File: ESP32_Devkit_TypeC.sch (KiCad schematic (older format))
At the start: 39 parts, among them J1 USB_C_Receptacle_USB2.0, J2 Conn_01x19, J3 Conn_01x19, Q1 SS8050, Q2 SS8050, SW1 EN, SW2 BOOT, U1 MP2451, U2 CH340G, U3 ESP32-PICO-D4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

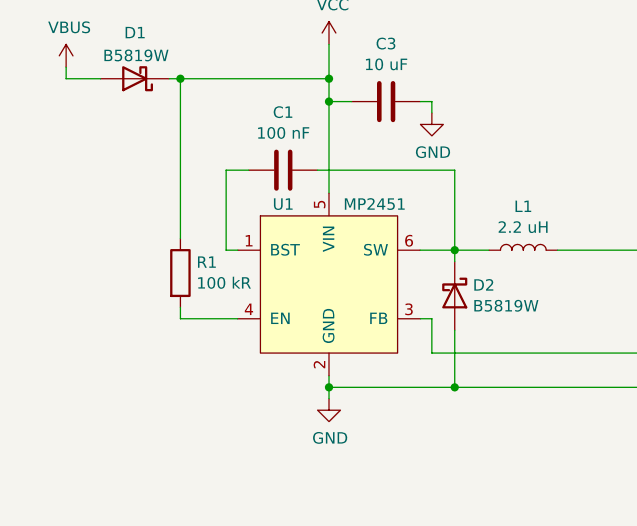
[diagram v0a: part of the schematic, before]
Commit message: Increase strength of step down enable pullup
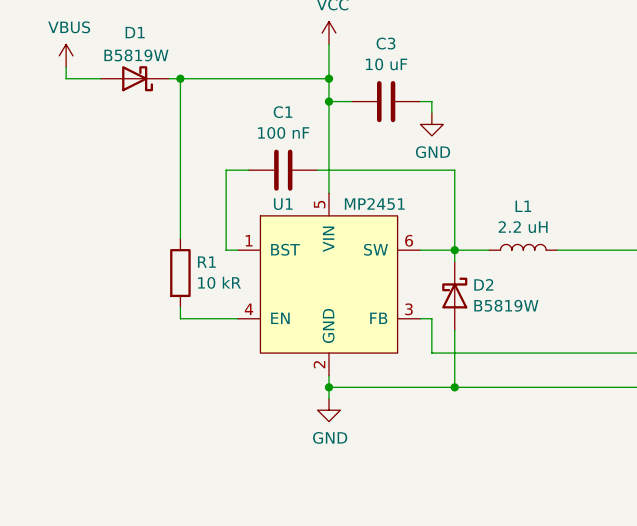
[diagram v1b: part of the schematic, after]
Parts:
- R1: value 100 kR -> 10 kR; LCSC C25741 -> C25744
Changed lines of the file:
@@
 P 1550 5100
 F 0 "R1" H 1620 5146 50  0000 L CNN
-F 1 "100 kR" H 1620 5055 50  0000 L CNN
+F 1 "10 kR" H 1620 5055 50  0000 L CNN
 F 2 "Resistor_SMD:R_0402_1005Metric" V 1480 5100 50  0001 C CNN
 F 3 "~" H 1550 5100 50  0001 C CNN
-F 4 "C25741" H 1550 5100 50  0001 C CNN "LCSC"
+F 4 "C25744" H 1550 5100 50  0001 C CNN "LCSC"
 	1    1550 5100
 	1    0    0    -1

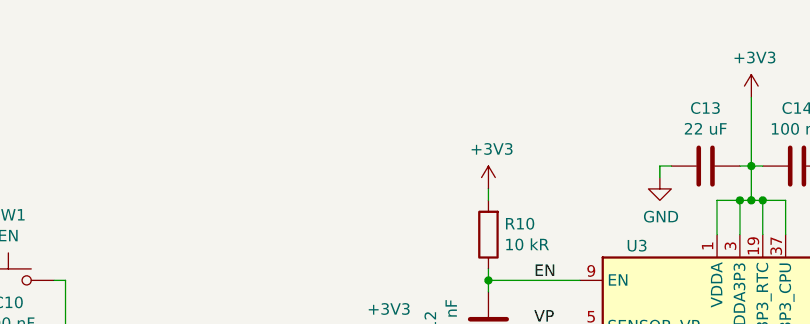
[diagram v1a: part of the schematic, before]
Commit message: Add tooling holes
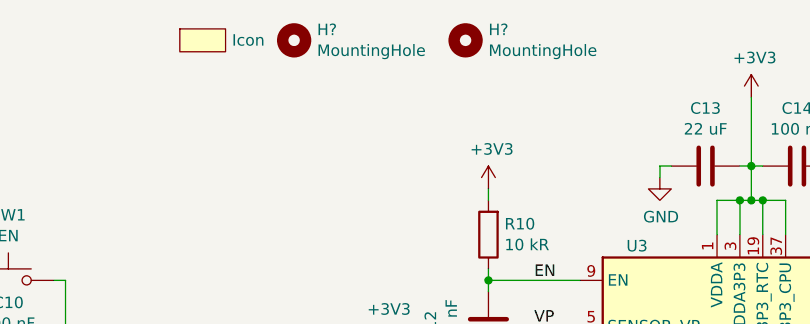
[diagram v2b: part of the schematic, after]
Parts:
- added H? (x2): MountingHole, ToolingHole:ToolingHole_JLCSMT, symbol Mechanical:MountingHole
- added I1: Icon, Signs:Danger_RF_Corona, symbol Icon:Icon
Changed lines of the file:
@@
 Wire Wire Line
 	3200 5000 3750 5000
+$Comp
+L Icon:Icon I1
+U 1 1 5F3C704C
+P 6400 600
+F 0 "I1" H 6400 600 50  0001 C CNN
+F 1 "Icon" H 6528 600 50  0000 L CNN
+F 2 "Signs:Danger_RF_Corona" H 6400 600 50  0001 C CNN
+F 3 "" H 6400 600 50  0001 C CNN
+	1    6400 600
+	1    0    0    -1
+$EndComp
+$Comp
+L Mechanical:MountingHole H?
+U 1 1 5F3DD188
+P 6800 600
+F 0 "H?" H 6900 646 50  0000 L CNN
+F 1 "MountingHole" H 6900 555 50  0000 L CNN
+F 2 "ToolingHole:ToolingHole_JLCSMT" H 6800 600 50  0001 C CNN
+F 3 "~" H 6800 600 50  0001 C CNN
+	1    6800 600
+	1    0    0    -1
+$EndComp
+$Comp
+L Mechanical:MountingHole H?
+U 1 1 5F3DDEDA
+P 7550 600
+F 0 "H?" H 7650 646 50  0000 L CNN
+F 1 "MountingHole" H 7650 555 50  0000 L CNN
+F 2 "ToolingHole:ToolingHole_JLCSMT" H 7550 600 50  0001 C CNN
+F 3 "~" H 7550 600 50  0001 C CNN
+	1    7550 600
+	1    0    0    -1
+$EndComp
 $EndSCHEMATC

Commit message: Add OSHW logo
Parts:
- added I?: Icon, Symbol:OSHW-Symbol_6.7x6mm_SilkScreen, symbol Icon:Icon
- gave numbers to parts that had none: 2
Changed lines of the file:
@@
 $EndComp
 $Comp
-L Mechanical:MountingHole H?
+L Mechanical:MountingHole H1
 U 1 1 5F3DD188
 P 6800 600
-F 0 "H?" H 6900 646 50  0000 L CNN
+F 0 "H1" H 6900 646 50  0000 L CNN
 F 1 "MountingHole" H 6900 555 50  0000 L CNN
 F 2 "ToolingHole:ToolingHole_JLCSMT" H 6800 600 50  0001 C CNN
@@
 $EndComp
 $Comp
-L Mechanical:MountingHole H?
+L Mechanical:MountingHole H2
 U 1 1 5F3DDEDA
 P 7550 600
-F 0 "H?" H 7650 646 50  0000 L CNN
+F 0 "H2" H 7650 646 50  0000 L CNN
 F 1 "MountingHole" H 7650 555 50  0000 L CNN
 F 2 "ToolingHole:ToolingHole_JLCSMT" H 7550 600 50  0001 C CNN
@@
 	1    0    0    -1
 $EndComp
+$Comp
+L Icon:Icon I?
+U 1 1 5F3FE9BA
+P 5950 600
+F 0 "I?" H 5950 600 50  0001 C CNN
+F 1 "Icon" H 6078 600 50  0000 L CNN
+F 2 "Symbol:OSHW-Symbol_6.7x6mm_SilkScreen" H 5950 600 50  0001 C CNN
+F 3 "" H 5950 600 50  0001 C CNN
+	1    5950 600
+	1    0    0    -1
+$EndComp

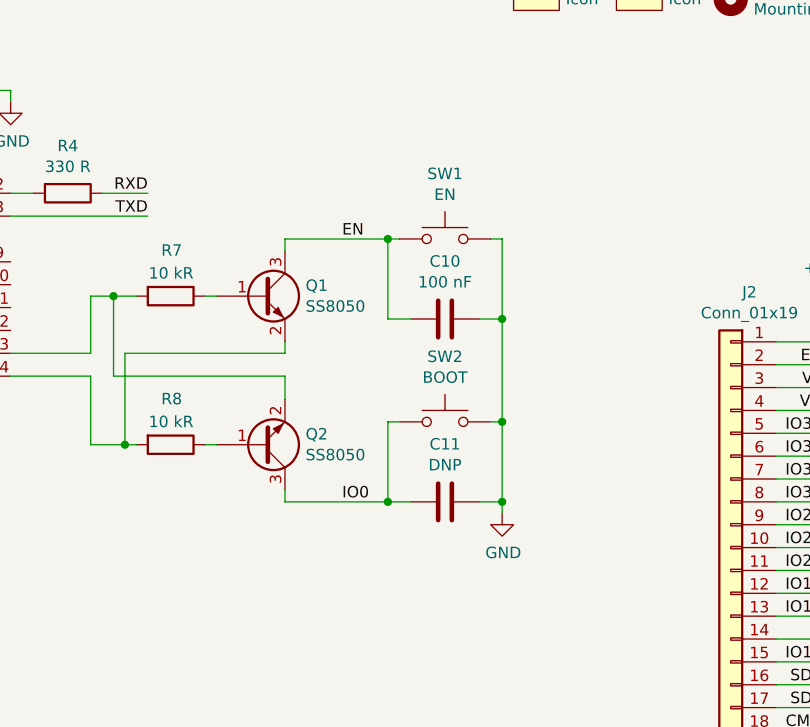
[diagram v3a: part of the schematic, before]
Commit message: Use ESP32 Pico D4 footprint
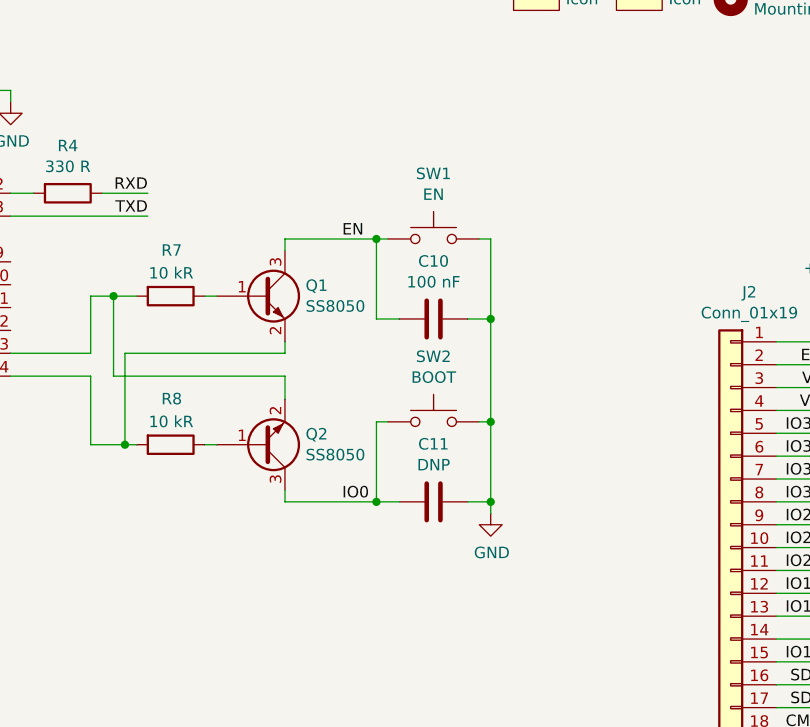
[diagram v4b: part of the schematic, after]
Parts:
- I2: renamed from I?; footprint Symbol:OSHW-Symbol_6.7x6mm_SilkScreen -> Signs:OSHW_icon_3.3x3
- U3: footprint Package_DFN_QFN:QFN-48-1EP_7x7mm_P0.5mm_EP5.3x5.3mm -> Package_ESP32:ESP32-Pico-D4
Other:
- moved on the sheet: C10, C11, SW1, SW2
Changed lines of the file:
@@
 L Switch:SW_Push SW1
 U 1 1 5ECA28F9
-P 5550 1650
-F 0 "SW1" H 5550 1935 50  0000 C CNN
-F 1 "EN" H 5550 1844 50  0000 C CNN
-F 2 "Button_Switch_SMD:SW_Push_SPST_NO_Alps_SKRK" H 5550 1850 50  0001 C CNN
-F 3 "~" H 5550 1850 50  0001 C CNN
-F 4 "C115357" H 5550 1650 50  0001 C CNN "LCSC"
-	1    5550 1650
+P 5500 1650
+F 0 "SW1" H 5500 1935 50  0000 C CNN
+F 1 "EN" H 5500 1844 50  0000 C CNN
+F 2 "Button_Switch_SMD:SW_Push_SPST_NO_Alps_SKRK" H 5500 1850 50  0001 C CNN
+F 3 "~" H 5500 1850 50  0001 C CNN
+F 4 "C115357" H 5500 1650 50  0001 C CNN "LCSC"
+	1    5500 1650
 	1    0    0    -1
 $EndComp
@@
 L Switch:SW_Push SW2
 U 1 1 5ECA6673
-P 5550 2450
-F 0 "SW2" H 5550 2735 50  0000 C CNN
-F 1 "BOOT" H 5550 2644 50  0000 C CNN
-F 2 "Button_Switch_SMD:SW_Push_SPST_NO_Alps_SKRK" H 5550 2650 50  0001 C CNN
-F 3 "~" H 5550 2650 50  0001 C CNN
-F 4 "C115357" H 5550 2450 50  0001 C CNN "LCSC"
-	1    5550 2450
+P 5500 2450
+F 0 "SW2" H 5500 2735 50  0000 C CNN
+F 1 "BOOT" H 5500 2644 50  0000 C CNN
+F 2 "Button_Switch_SMD:SW_Push_SPST_NO_Alps_SKRK" H 5500 2650 50  0001 C CNN
+F 3 "~" H 5500 2650 50  0001 C CNN
+F 4 "C115357" H 5500 2450 50  0001 C CNN "LCSC"
+	1    5500 2450
 	1    0    0    -1
 $EndComp
@@
 F 0 "U3" H 8300 4600 50  0000 C CNN
 F 1 "ESP32-PICO-D4" H 9350 4600 50  0000 C CNN
-F 2 "Package_DFN_QFN:QFN-48-1EP_7x7mm_P0.5mm_EP5.3x5.3mm" H 8850 1350 50  0001 C CNN
+F 2 "Package_ESP32:ESP32-Pico-D4" H 8850 1350 50  0001 C CNN
 F 3 "https://www.espressif.com/sites/default/files/documentation/esp32-pico-d4_datasheet_en.pdf" H 9100 2050 50  0001 C CNN
 F 4 "C193707" H 8850 3050 50  0001 C CNN "LCSC"
@@
 L Device:C C11
 U 1 1 5EF0984E
-P 5550 2800
-F 0 "C11" V 5298 2800 50  0000 C CNN
-F 1 "DNP" V 5389 2800 50  0000 C CNN
-F 2 "Capacitor_SMD:C_0402_1005Metric" H 5588 2650 50  0001 C CNN
-F 3 "~" H 5550 2800 50  0001 C CNN
-	1    5550 2800
+P 5500 2800
+F 0 "C11" V 5248 2800 50  0000 C CNN
+F 1 "DNP" V 5339 2800 50  0000 C CNN
+F 2 "Capacitor_SMD:C_0402_1005Metric" H 5538 2650 50  0001 C CNN
+F 3 "~" H 5500 2800 50  0001 C CNN
+	1    5500 2800
 	0    1    1    0
 $EndComp
@@
 L Device:C C10
 U 1 1 5EF13A64
-P 5550 2000
-F 0 "C10" V 5298 2000 50  0000 C CNN
-F 1 "100 nF" V 5389 2000 50  0000 C CNN
-F 2 "Capacitor_SMD:C_0402_1005Metric" H 5588 1850 50  0001 C CNN
-F 3 "~" H 5550 2000 50  0001 C CNN
-F 4 "C1525" H 5550 2000 50  0001 C CNN "LCSC"
-	1    5550 2000
+P 5500 2000
+F 0 "C10" V 5248 2000 50  0000 C CNN
+F 1 "100 nF" V 5339 2000 50  0000 C CNN
+F 2 "Capacitor_SMD:C_0402_1005Metric" H 5538 1850 50  0001 C CNN
+F 3 "~" H 5500 2000 50  0001 C CNN
+F 4 "C1525" H 5500 2000 50  0001 C CNN "LCSC"
+	1    5500 2000
 	0    1    1    0
 $EndComp
 Wire Wire Line
-	5750 2450 5800 2450
-Wire Wire Line
-	5800 2450 5800 2800
-Wire Wire Line
-	5800 2800 5700 2800
-Wire Wire Line
-	5400 2800 5300 2800
-Wire Wire Line
-	5300 2800 5300 2450
-Wire Wire Line
-	5300 2450 5350 2450
-Wire Wire Line
-	5350 1650 5300 1650
-Wire Wire Line
-	5300 1650 5300 2000
-Wire Wire Line
-	5300 2000 5400 2000
-Wire Wire Line
-	5750 1650 5800 1650
-Wire Wire Line
-	5800 1650 5800 2000
-Wire Wire Line
-	5700 2000 5800 2000
+	5700 2450 5750 2450
+Wire Wire Line
+	5750 2450 5750 2800
+Wire Wire Line
+	5750 2800 5650 2800
+Wire Wire Line
+	5350 2800 5250 2800
+Wire Wire Line
+	5250 2800 5250 2450
+Wire Wire Line
+	5250 2450 5300 2450
+Wire Wire Line
+	5300 1650 5250 1650
+Wire Wire Line
+	5250 1650 5250 2000
+Wire Wire Line
+	5250 2000 5350 2000
+Wire Wire Line
+	5700 1650 5750 1650
+Wire Wire Line
+	5750 1650 5750 2000
+Wire Wire Line
+	5650 2000 5750 2000
 $Comp
 L Device:C C12
@@
 	4850 2750 4850 2800
 Wire Wire Line
-	4850 2800 5300 2800
-Connection ~ 5300 2800
-Wire Wire Line
 	4850 1700 4850 1650
-Wire Wire Line
-	4850 1650 5300 1650
-Connection ~ 5300 1650
 $Comp
 L Device:R R7
@@
 L power:GND #PWR0123
 U 1 1 5F0F7667
-P 5800 2850
-F 0 "#PWR0123" H 5800 2600 50  0001 C CNN
-F 1 "GND" H 5805 2677 50  0000 C CNN
-F 2 "" H 5800 2850 50  0001 C CNN
-F 3 "" H 5800 2850 50  0001 C CNN
-	1    5800 2850
-	1    0    0    -1
-$EndComp
-Wire Wire Line
-	5800 2850 5800 2800
-Connection ~ 5800 2800
-Wire Wire Line
-	5800 2450 5800 2000
-Connection ~ 5800 2450
-Connection ~ 5800 2000
+P 5750 2850
+F 0 "#PWR0123" H 5750 2600 50  0001 C CNN
+F 1 "GND" H 5755 2677 50  0000 C CNN
+F 2 "" H 5750 2850 50  0001 C CNN
+F 3 "" H 5750 2850 50  0001 C CNN
+	1    5750 2850
+	1    0    0    -1
+$EndComp
+Wire Wire Line
+	5750 2850 5750 2800
+Connection ~ 5750 2800
+Wire Wire Line
+	5750 2450 5750 2000
+Connection ~ 5750 2450
+Connection ~ 5750 2000
 Text Label 5100 1650 0    50   ~ 0
 EN
@@
 $EndComp
 $Comp
-L Icon:Icon I?
+L Icon:Icon I2
 U 1 1 5F3FE9BA
 P 5950 600
-F 0 "I?" H 5950 600 50  0001 C CNN
+F 0 "I2" H 5950 600 50  0001 C CNN
 F 1 "Icon" H 6078 600 50  0000 L CNN
-F 2 "Symbol:OSHW-Symbol_6.7x6mm_SilkScreen" H 5950 600 50  0001 C CNN
+F 2 "Signs:OSHW_icon_3.3x3" H 5950 600 50  0001 C CNN
 F 3 "" H 5950 600 50  0001 C CNN
 	1    5950 600
 	1    0    0    -1
 $EndComp
+Connection ~ 5250 1650
+Connection ~ 5250 2800
+Wire Wire Line
+	4850 1650 5250 1650
+Wire Wire Line
+	4850 2800 5250 2800
 $EndSCHEMATC
